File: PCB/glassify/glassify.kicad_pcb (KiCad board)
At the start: 2 copper layers, 60 x 56 mm, 16 parts, among them J1 Conn_02x09_Odd_Even

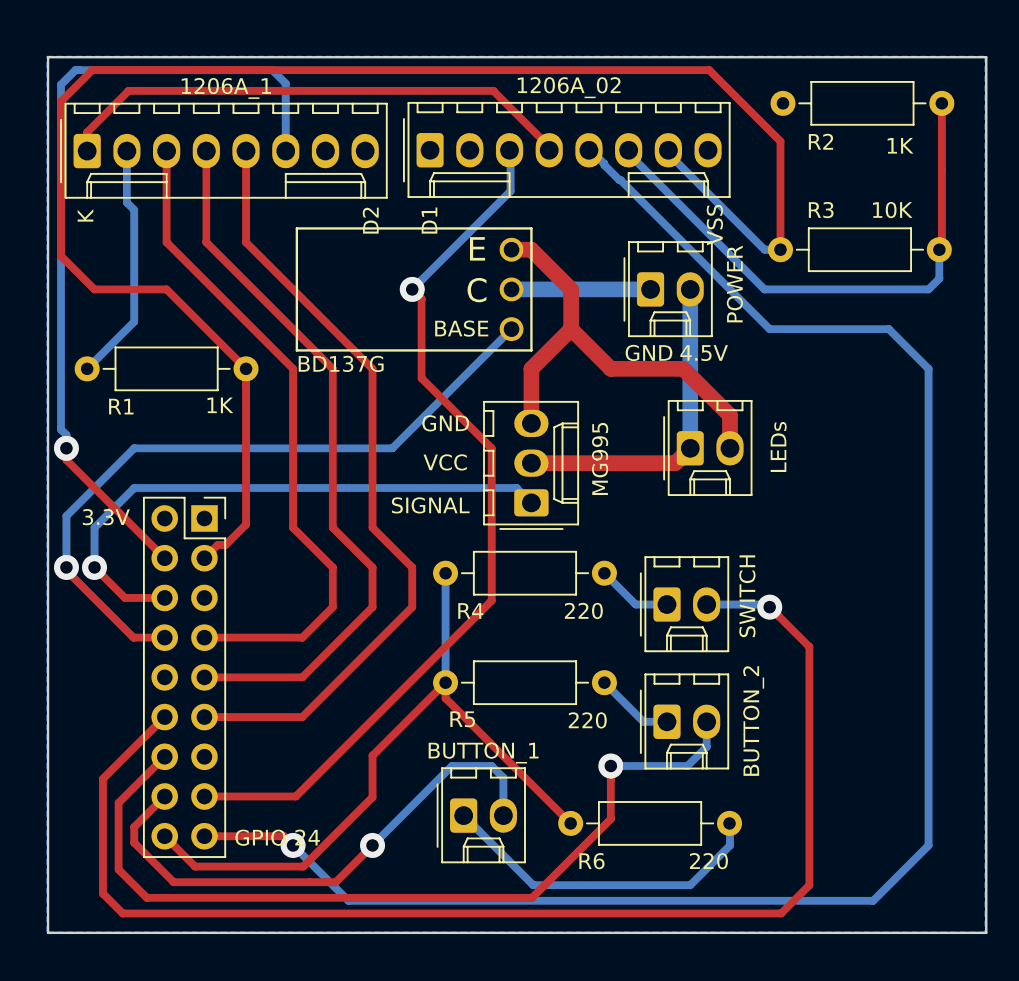
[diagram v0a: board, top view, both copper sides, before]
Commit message: Moving traces further from edges, moving some traces from top layer to bottom one.
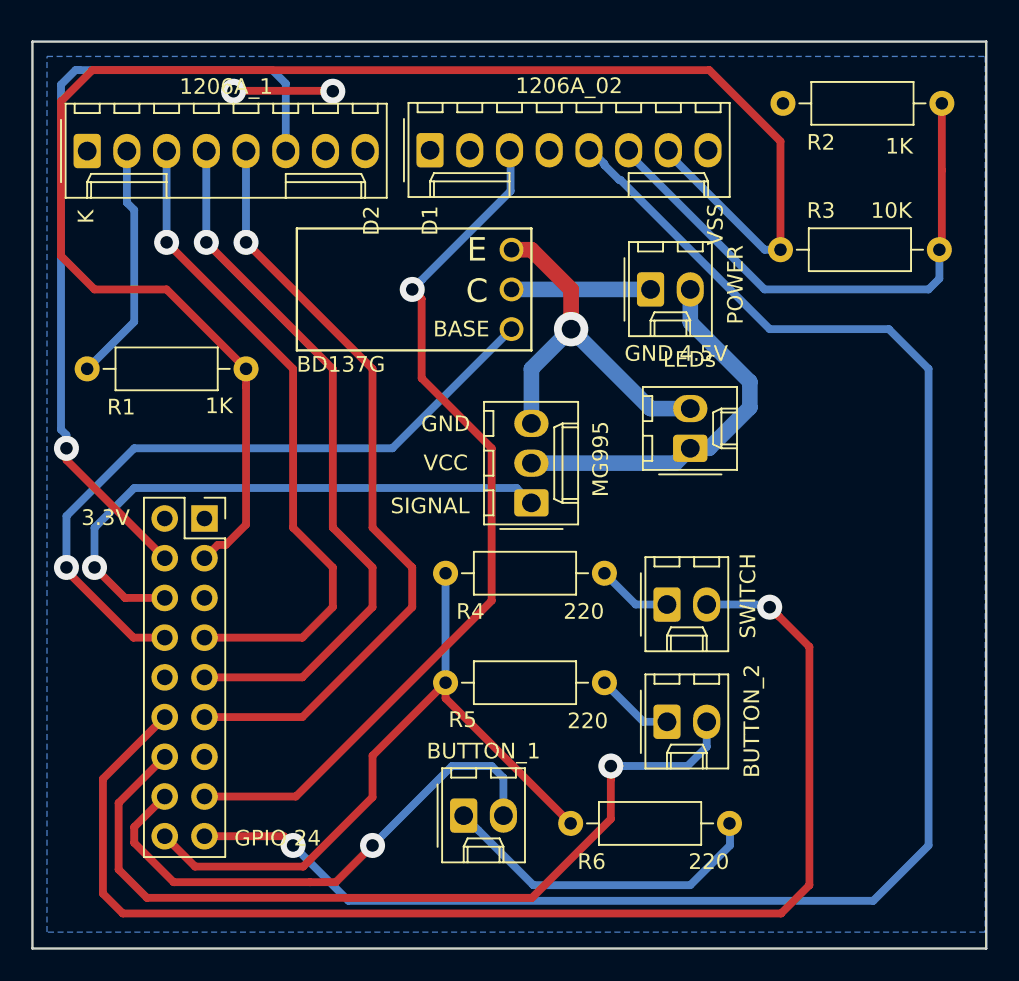
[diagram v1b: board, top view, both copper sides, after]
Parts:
- turned LEDs to 90 degrees
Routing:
- net Net-(1206A_01x08_Male1-Pad1): track 33.6 -> 0.00 mm
- net (no net): track 0.00 -> 6.39 mm, vias 0 -> 2
- net Net-(2mm_pitch4-Pad3): track 29.0 -> 24.2 mm, vias 0 -> 1
- net Net-(2mm_pitch4-Pad2): track 20.7 -> 24.6 mm
- net Net-(1206A_01x08_Male1-Pad5): vias 0 -> 1
- net Net-(1206A_01x08_Male1-Pad4): vias 0 -> 1
- net Net-(1206A_01x08_Male1-Pad3): vias 0 -> 1
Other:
- board size 60 x 56 mm -> 61 x 58 mm
- net class Default: trace_width 0.5 -> 1
- net class Power removed
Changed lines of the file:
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@@
     (thickness 1.6)
     (drawings 21)
-    (tracks 172)
+    (tracks 178)
     (zones 0)
     (modules 16)
@@
   )
   (setup
-    (last_trace_width 0.5)
+    (last_trace_width 1)
     (trace_clearance 0.5)
     (zone_clearance 0.508)
@@
   (net_class Default "This is the default net class."
     (clearance 0.5)
-    (trace_width 0.5)
+    (trace_width 1)
     (via_dia 1.2)
     (via_drill 0.8)
     (uvia_dia 0.3)
     (uvia_drill 0.1)
+    (diff_pair_gap 0.25)
+    (diff_pair_width 0.5)
     (add_net "Net-(1206A_01x08_Male1-Pad1)")
     (add_net "Net-(1206A_01x08_Male1-Pad2)")
@@
     (add_net "Net-(J1-Pad10)")
     (add_net "Net-(J1-Pad13)")
-  )
-  (net_class Power ""
-    (clearance 0.5)
-    (trace_width 1)
-    (via_dia 1.2)
-    (via_drill 0.8)
-    (uvia_dia 0.3)
-    (uvia_drill 0.1)
   )
   (module Connector_Molex:Molex_KK-254_AE-6410-08A_1x08_P2.54mm_Vertical (layer F.Cu)
@@
   )
   (module Connector_Molex:Molex_KK-254_AE-6410-02A_1x02_P2.54mm_Vertical (layer F.Cu)
-    (at 167.64 99.06)
+    (at 167.64 99.06 90)
     (descr "Molex KK-254 Interconnect System, old/engineering part number: AE-6410-02A example for new part number: 22-27-2021, 2 Pins (http://www.molex.com/pdm_docs/sd/022272021_sd.pdf), generated with kicad-footprint-generator")
     (tags "connector Molex KK-254 side entry")
-    (fp_text reference LEDs (at 5.68 -0.05 90) (layer F.SilkS)
-      (effects (font (size 1 1) (thickness 0.15)))
-    )
-    (fp_text value 2mm_pitch (at 1.27 4.08) (layer F.Fab) hide
-      (effects (font (size 1 1) (thickness 0.15)))
-    )
-    (fp_text user %R (at 1.27 -2.22) (layer F.Fab)
+    (fp_text reference LEDs (at 5.68 -0.05 180) (layer F.SilkS)
+      (effects (font (size 1 1) (thickness 0.15)))
+    )
+    (fp_text value 2mm_pitch (at 1.27 4.08 90) (layer F.Fab) hide
+      (effects (font (size 1 1) (thickness 0.15)))
+    )
+    (fp_text user %R (at 1.27 -2.22 90) (layer F.Fab)
       (effects (font (size 1 1) (thickness 0.15)))
     )
@@
     (fp_line (start -1.27 2.88) (end 3.81 2.88) (layer F.Fab) (width 0.1))
     (fp_line (start -1.27 -2.92) (end -1.27 2.88) (layer F.Fab) (width 0.1))
-    (pad 2 thru_hole oval (at 2.54 0) (size 1.74 2.2) (drill 1.2) (layers *.Cu *.Mask)
+    (pad 2 thru_hole oval (at 2.54 0 90) (size 1.74 2.2) (drill 1.2) (layers *.Cu *.Mask)
       (net 23 "Net-(2mm_pitch4-Pad3)"))
-    (pad 1 thru_hole roundrect (at 0 0) (size 1.74 2.2) (drill 1.2) (layers *.Cu *.Mask) (roundrect_rratio 0.143678)
+    (pad 1 thru_hole roundrect (at 0 0 90) (size 1.74 2.2) (drill 1.2) (layers *.Cu *.Mask) (roundrect_rratio 0.143678)
       (net 22 "Net-(2mm_pitch4-Pad2)"))
     (model ${KISYS3DMOD}/Connector_Molex.3dshapes/Molex_KK-254_AE-6410-02A_1x02_P2.54mm_Vertical.wrl
@@
     (effects (font (size 1 1) (thickness 0.25)))
   )
-  (gr_line (start 126.57 74.05) (end 186.57 74.05) (layer Edge.Cuts) (width 0.15))
-  (gr_line (start 126.57 130.05) (end 126.57 74.05) (layer Edge.Cuts) (width 0.15))
-  (gr_line (start 186.57 130.05) (end 126.57 130.05) (layer Edge.Cuts) (width 0.15))
-  (gr_line (start 186.57 74.05) (end 186.57 130.05) (layer Edge.Cuts) (width 0.15))
-  (segment (start 158.62 79.77) (end 158.62 80) (width 0.5) (layer F.Cu) (net 1))
-  (segment (start 155.05 76.2) (end 158.62 79.77) (width 0.5) (layer F.Cu) (net 1))
-  (segment (start 131.72 76.2) (end 155.05 76.2) (width 0.5) (layer F.Cu) (net 1))
-  (segment (start 129.07 78.85) (end 131.72 76.2) (width 0.5) (layer F.Cu) (net 1))
-  (segment (start 129.07 80.05) (end 129.07 78.85) (width 0.5) (layer F.Cu) (net 1))
+  (gr_line (start 125.57 73.05) (end 186.57 73.05) (layer Edge.Cuts) (width 0.15))
+  (gr_line (start 125.57 131.05) (end 125.57 73.05) (layer Edge.Cuts) (width 0.15))
+  (gr_line (start 186.57 131.05) (end 125.57 131.05) (layer Edge.Cuts) (width 0.15))
+  (gr_line (start 186.57 73.05) (end 186.57 131.05) (layer Edge.Cuts) (width 0.15))
+  (via (at 144.78 76.22501) (size 1.6) (drill 0.8) (layers F.Cu B.Cu) (net 0))
+  (segment (start 138.43 76.2) (end 144.75499 76.2) (width 0.5) (layer F.Cu) (net 0))
+  (segment (start 144.75499 76.2) (end 144.78 76.22501) (width 0.5) (layer F.Cu) (net 0))
+  (via (at 138.43 76.22501) (size 1.6) (drill 0.8) (layers F.Cu B.Cu) (net 0))
+  (segment (start 138.43 76.2) (end 138.43 76.22501) (width 0.5) (layer F.Cu) (net 0))
   (segment (start 132.08 90.97) (end 129.07 93.98) (width 0.5) (layer B.Cu) (net 2))
   (segment (start 132.08 83.82) (end 132.08 90.97) (width 0.5) (layer B.Cu) (net 2))
@@
   (segment (start 131.61 83.35) (end 132.08 83.82) (width 0.5) (layer B.Cu) (net 2))
   (segment (start 134.15 85.89) (end 142.24 93.98) (width 0.5) (layer F.Cu) (net 3))
-  (segment (start 134.15 80.05) (end 134.15 85.89) (width 0.5) (layer F.Cu) (net 3))
   (segment (start 142.24 93.98) (end 142.24 104.14) (width 0.5) (layer F.Cu) (net 3))
   (segment (start 142.24 104.14) (end 144.78 106.68) (width 0.5) (layer F.Cu) (net 3))
@@
   (segment (start 144.78 109.22) (end 142.83 111.17) (width 0.5) (layer F.Cu) (net 3))
   (segment (start 142.83 111.17) (end 136.57 111.17) (width 0.5) (layer F.Cu) (net 3))
+  (via (at 134.15 85.89) (size 1.6) (drill 0.8) (layers F.Cu B.Cu) (net 3))
+  (segment (start 134.15 80.05) (end 134.15 85.89) (width 0.5) (layer B.Cu) (net 3))
   (segment (start 137.41 113.71) (end 136.57 113.71) (width 0.25) (layer B.Cu) (net 4))
   (segment (start 144.78 93.98) (end 144.78 104.14) (width 0.5) (layer F.Cu) (net 4))
-  (segment (start 136.69 80.05) (end 136.69 85.89) (width 0.5) (layer F.Cu) (net 4))
   (segment (start 136.69 85.89) (end 144.78 93.98) (width 0.5) (layer F.Cu) (net 4))
   (segment (start 144.78 104.14) (end 147.32 106.68) (width 0.5) (layer F.Cu) (net 4))
@@
   (segment (start 147.32 109.22) (end 142.83 113.71) (width 0.5) (layer F.Cu) (net 4))
   (segment (start 142.83 113.71) (end 136.57 113.71) (width 0.5) (layer F.Cu) (net 4))
+  (segment (start 136.69 80.05) (end 136.69 85.89) (width 0.5) (layer B.Cu) (net 4))
+  (via (at 136.69 85.89) (size 1.6) (drill 0.8) (layers F.Cu B.Cu) (net 4))
   (segment (start 142.83 116.25) (end 136.57 116.25) (width 0.5) (layer F.Cu) (net 5))
   (segment (start 139.23 85.89) (end 147.32 93.98) (width 0.5) (layer F.Cu) (net 5))
-  (segment (start 139.23 80.05) (end 139.23 85.89) (width 0.5) (layer F.Cu) (net 5))
   (segment (start 147.32 93.98) (end 147.32 104.14) (width 0.5) (layer F.Cu) (net 5))
   (segment (start 147.32 104.14) (end 149.86 106.68) (width 0.5) (layer F.Cu) (net 5))
   (segment (start 149.86 106.68) (end 149.86 109.22) (width 0.5) (layer F.Cu) (net 5))
   (segment (start 149.86 109.22) (end 142.83 116.25) (width 0.5) (layer F.Cu) (net 5))
+  (segment (start 139.23 80.05) (end 139.23 85.89) (width 0.5) (layer B.Cu) (net 5))
+  (via (at 139.23 85.89) (size 1.6) (drill 0.8) (layers F.Cu B.Cu) (net 5))
   (segment (start 134.029978 106.09) (end 134.03 106.09) (width 0.5) (layer B.Cu) (net 6))
   (segment (start 134.03 106.09) (end 127.745 99.805) (width 0.5) (layer F.Cu) (net 6))
@@
   (segment (start 129.54 104.14) (end 132.08 101.6) (width 0.5) (layer B.Cu) (net 21))
   (segment (start 156.53 101.6) (end 157.48 102.55) (width 0.5) (layer B.Cu) (net 21))
-  (segment (start 166.69 100.01) (end 167.64 99.06) (width 1) (layer F.Cu) (net 22))
-  (segment (start 157.48 100.01) (end 166.69 100.01) (width 1) (layer F.Cu) (net 22))
-  (segment (start 167.64 99.06) (end 167.64 88.9) (width 1) (layer B.Cu) (net 22))
+  (segment (start 167.64 91) (end 171.45 94.81) (width 1) (layer B.Cu) (net 22))
+  (segment (start 167.64 88.9) (end 167.64 91) (width 1) (layer B.Cu) (net 22))
+  (segment (start 171.45 96.45) (end 168.84 99.06) (width 1) (layer B.Cu) (net 22))
+  (segment (start 168.84 99.06) (end 167.64 99.06) (width 1) (layer B.Cu) (net 22))
+  (segment (start 171.45 94.81) (end 171.45 96.45) (width 1) (layer B.Cu) (net 22))
+  (segment (start 166.69 100.01) (end 167.64 99.06) (width 1) (layer B.Cu) (net 22))
+  (segment (start 157.48 100.01) (end 166.69 100.01) (width 1) (layer B.Cu) (net 22))
   (segment (start 156.21 86.36) (end 157.48 86.36) (width 1) (layer F.Cu) (net 23))
   (segment (start 157.48 86.36) (end 160.02 88.9) (width 1) (layer F.Cu) (net 23))
   (segment (start 160.02 88.9) (end 160.02 91.44) (width 1) (layer F.Cu) (net 23))
-  (segment (start 157.48 93.98) (end 157.48 97.47) (width 1) (layer F.Cu) (net 23))
-  (segment (start 160.02 91.44) (end 157.48 93.98) (width 1) (layer F.Cu) (net 23))
-  (segment (start 170.18 96.96) (end 167.2 93.98) (width 1) (layer F.Cu) (net 23))
-  (segment (start 170.18 99.06) (end 170.18 96.96) (width 1) (layer F.Cu) (net 23))
-  (segment (start 167.2 93.98) (end 162.56 93.98) (width 1) (layer F.Cu) (net 23))
-  (segment (start 162.56 93.98) (end 160.02 91.44) (width 1) (layer F.Cu) (net 23))
+  (via (at 160.02 91.44) (size 2.2) (drill 1.2) (layers F.Cu B.Cu) (net 23) (status 1000000))
+  (segment (start 167.64 96.52) (end 165.1 96.52) (width 1) (layer B.Cu) (net 23))
+  (segment (start 165.1 96.52) (end 160.02 91.44) (width 1) (layer B.Cu) (net 23))
+  (segment (start 157.48 93.98) (end 160.02 91.44) (width 1) (layer B.Cu) (net 23))
+  (segment (start 157.48 97.47) (end 157.48 93.98) (width 1) (layer B.Cu) (net 23))
   (segment (start 165.1 88.9) (end 156.540001 88.9) (width 1) (layer B.Cu) (net 24))
   (via (at 127.745 106.68) (size 1.6) (drill 0.8) (layers F.Cu B.Cu) (net 25))
